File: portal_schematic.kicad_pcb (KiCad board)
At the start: 2 copper layers, 101.6 x 53.3 mm, 93 parts, among them J1 RS485_1, J2 ATX_PW_SW, J3 Sensor, J4 RS485_1_Config, J5 CAM_SW, J6 ILLUM_SW, J7 RS232_1, J8 RS232_2, K1 Relay_PW_SW, P1 Power, P10 CONN_01X01, P11 CONN_01X01, P12 CONN_01X01, P13 CONN_01X01, P2 Analog, P3 Analog, P4 Digital, P5 PWM, P6 PWM, P7 Communication, P8 CONN_01X01, P9 CONN_01X01, Q1 BSS123LT1, Q10 FDN340P, Q11 FDN340P, Q2 STP16NF06L, Q3 STP16NF06L, Q4 FDN340P, Q5 FDN340P, Q6 FDN340P, Q7 FDN340P, Q8 FDN340P, Q9 FDN340P, SW1 SW_UART1, U1 LTV-817S, U2 LTV-817S, U3 MAX481E, U4 MP1584, U5 LTV-817S, U6 LTV-817S, U7 MAX3232

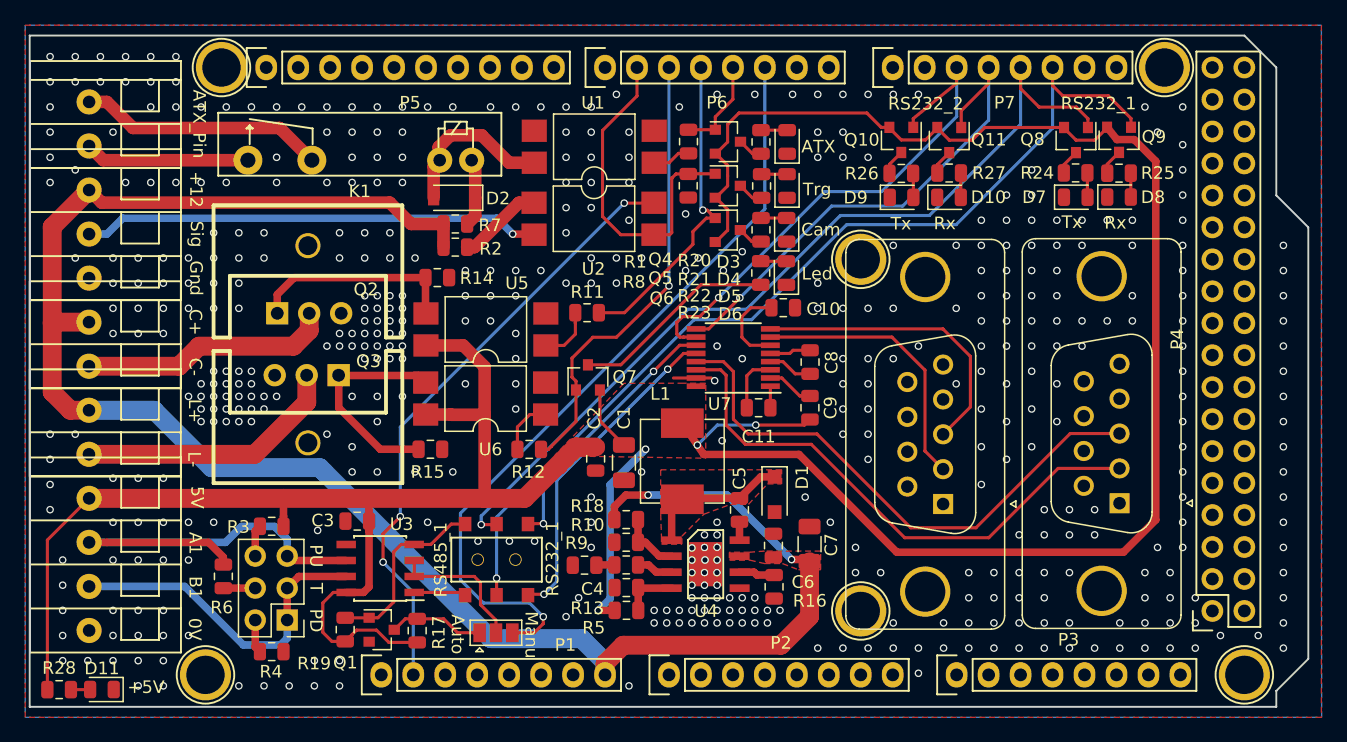
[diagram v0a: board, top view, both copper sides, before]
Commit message: Modified: visual enhancement is added
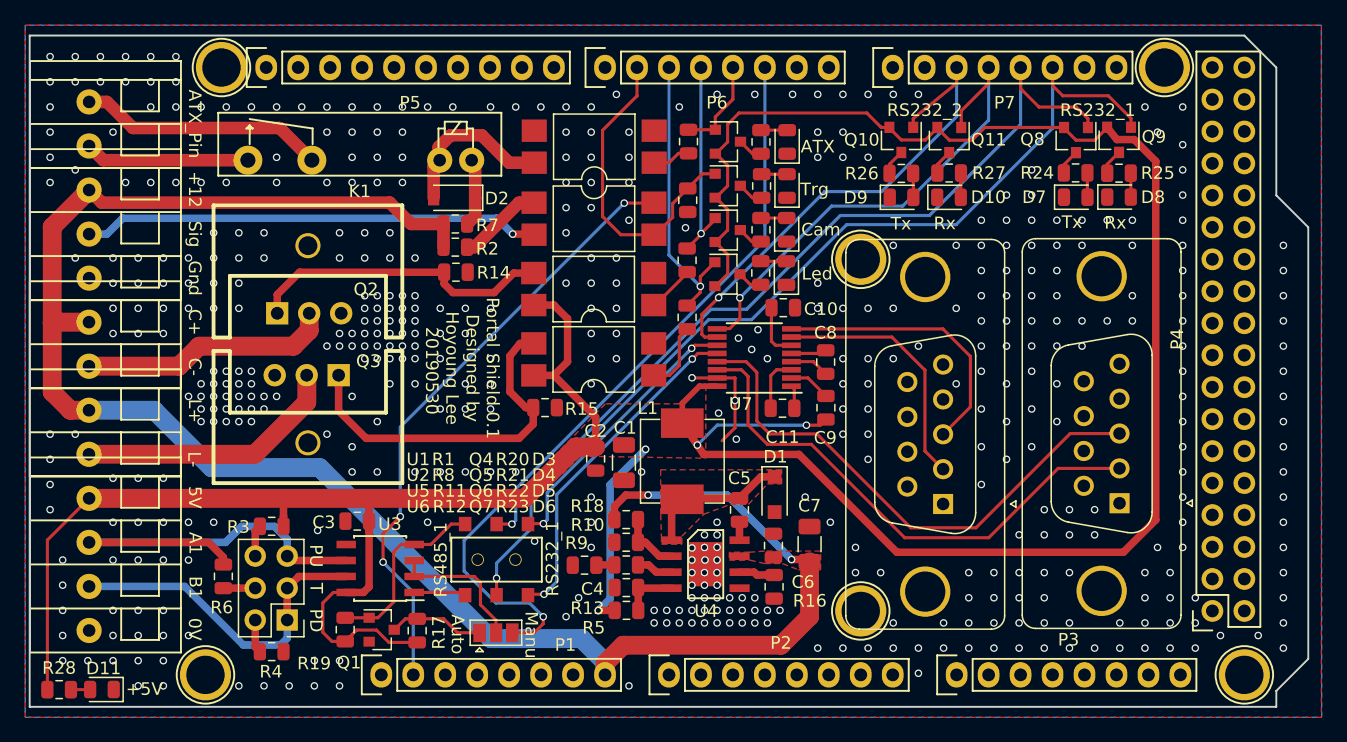
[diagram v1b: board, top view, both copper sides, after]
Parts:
- moved R12 16.4 mm to (155.6, 90.7), turned to 270 degrees
- moved Q7 13.8 mm to (158.8, 87.3), turned to 0 degrees
- moved R15 9.69 mm to (144.3, 97.9)
- moved U5 9.15 mm to (148.2, 88.5)
- moved U6 9.14 mm to (148.2, 94.1)
- moved R11 8.98 mm to (155.6, 86.2), turned to 270 degrees
- moved C11 1.90 mm to (163.2, 97.9)
- moved U7 1.67 mm to (161.0, 93.9)
- moved R14 1.54 mm to (137.2, 87.1)
- moved C9 1.27 mm to (166.7, 97.9)
- moved C8 1.24 mm to (166.6, 94.3)
- moved R8 1.15 mm to (155.7, 81.4)
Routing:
- net Net-(Q7-Pad3): track 16.4 -> 2.00 mm
- net /5(ILLUM_SW): track 36.3 -> 22.8 mm
- net Net-(Q3-Pad1): track 17.4 -> 28.6 mm
- net /4(CAM_SW): track 25.6 -> 16.5 mm
- net Net-(Q2-Pad1): track 16.7 -> 24.5 mm
- net GND: track 3.00 -> 8.83 mm, vias 470 -> 481
- net Net-(C10-Pad2): track 6.81 -> 4.39 mm
- net /18(Tx1): track 70.9 -> 68.8 mm
- net /16(Tx2): track 41.9 -> 39.9 mm
- net /6(TICK): track 27.1 -> 25.3 mm
- net Net-(J7-Pad2): track 43.8 -> 42.0 mm
- net Net-(J8-Pad3): track 23.9 -> 22.2 mm
- net Net-(J8-Pad2): track 21.8 -> 20.2 mm
- net +5V: track 255.8 -> 257.5 mm
- net Net-(J7-Pad3): track 44.4 -> 42.8 mm
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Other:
- board text added: "Portal Shield 0.1 Designed by Hoyoung Lee 20190530"

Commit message: The option of switching/powering in Cam and Illumination are added
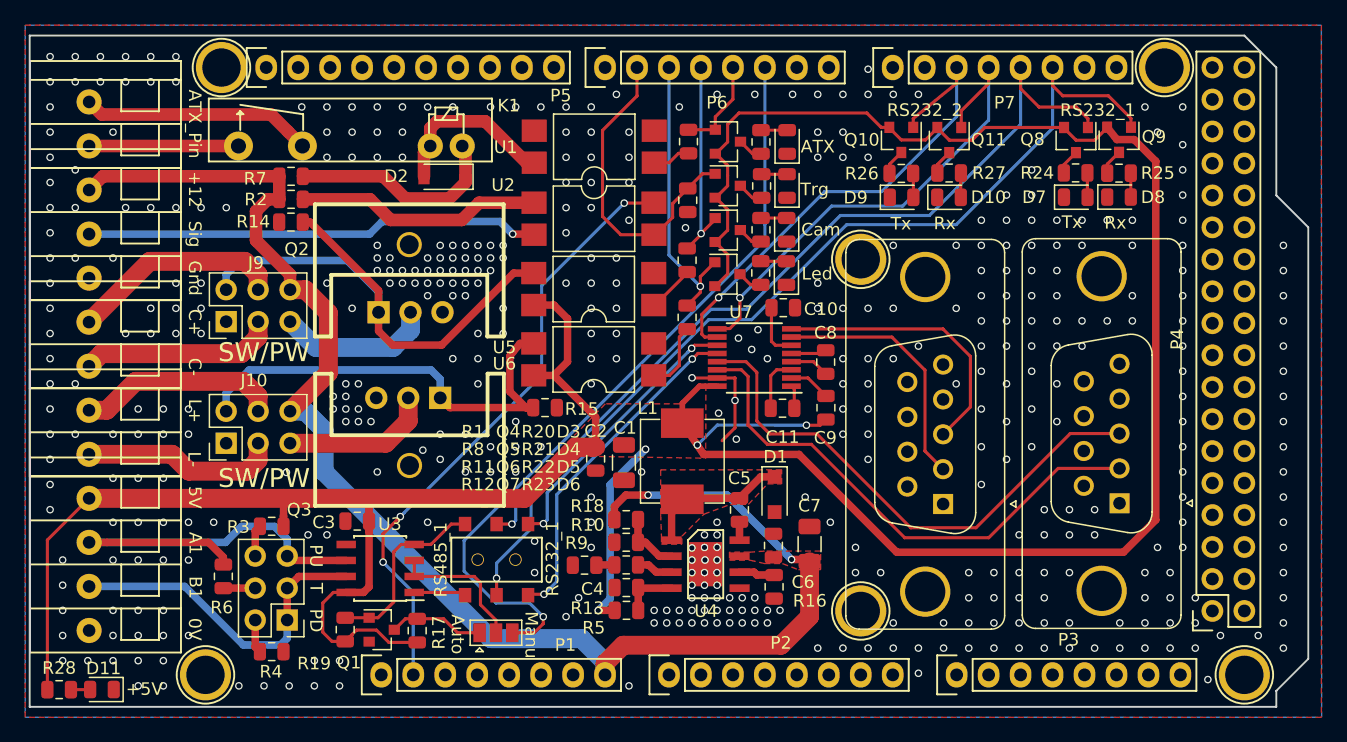
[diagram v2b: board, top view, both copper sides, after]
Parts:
- added J10: ILLUM_SW_CONFIG, Connector_PinHeader_2.54mm:PinHeader_2x03_P2.54mm_Vertical, F.Cu at (119.0, 100.7)
- added J9: CAM_SW_CONFIG, Connector_PinHeader_2.54mm:PinHeader_2x03_P2.54mm_Vertical, F.Cu at (119.0, 91.1)
- K1: value Relay_PW_SW -> PA1A-12
- moved R14 13.7 mm to (124.1, 83.2), turned to 0 degrees
- moved R2 13.6 mm to (124.2, 81.3)
- moved R7 13.6 mm to (124.2, 79.5)
- moved Q3 8.27 mm to (133.6, 100.1)
- moved Q2 8.05 mm to (133.5, 87.3)
- moved D2 1.84 mm to (136.4, 79.5)
- moved K1 1.36 mm to (128.9, 75.8)
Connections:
- J5 pad 2: /Vin(12V) -> Net-(J5-Pad2)
- J6 pad 1: Net-(J6-Pad1) -> Net-(J10-Pad3)
- J6 pad 2: /Vin(12V) -> Net-(J10-Pad4)
- Q2 pad 2: Net-(J5-Pad1) -> Net-(J9-Pad5)
- Q3 pad 2: Net-(J6-Pad1) -> Net-(J10-Pad5)
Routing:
- net /Vin(12V): track 147.3 -> 118.3 mm
- net Net-(J6-Pad1): track 21.1 -> 0.00 mm
- net Net-(J9-Pad2): track 24.5 -> 43.1 mm
- net Net-(J5-Pad2): track 0.00 -> 17.1 mm
- net Net-(J10-Pad4): track 0.00 -> 16.1 mm
- net Net-(J10-Pad3): track 0.00 -> 15.7 mm
- net Net-(R2-Pad1): track 6.78 -> 19.6 mm
- net Net-(J9-Pad5): track 0.00 -> 12.4 mm
- net Net-(J10-Pad5): track 0.00 -> 12.0 mm
- net Net-(D2-Pad1): track 5.45 -> 17.2 mm
- net Net-(J10-Pad2): track 28.6 -> 36.3 mm
- net Net-(J5-Pad1): track 20.0 -> 15.6 mm
- net Net-(J2-Pad2): track 19.6 -> 18.4 mm
- net Net-(J2-Pad1): track 13.1 -> 11.9 mm
- net Net-(D2-Pad2): track 13.1 -> 13.9 mm
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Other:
- board text added: "Portal Shield 0.1(20190530) Designed by Hoyoung Lee"
- board text added: "SW/PW"
- board text removed: "Portal Shield 0.1 Designed by Hoyoung Lee 20190530"
